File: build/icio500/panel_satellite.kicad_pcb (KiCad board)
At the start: 2 copper layers, 38.1 x 133.3 mm, 30 parts, among them J1 ?, U1 IS31FL3236

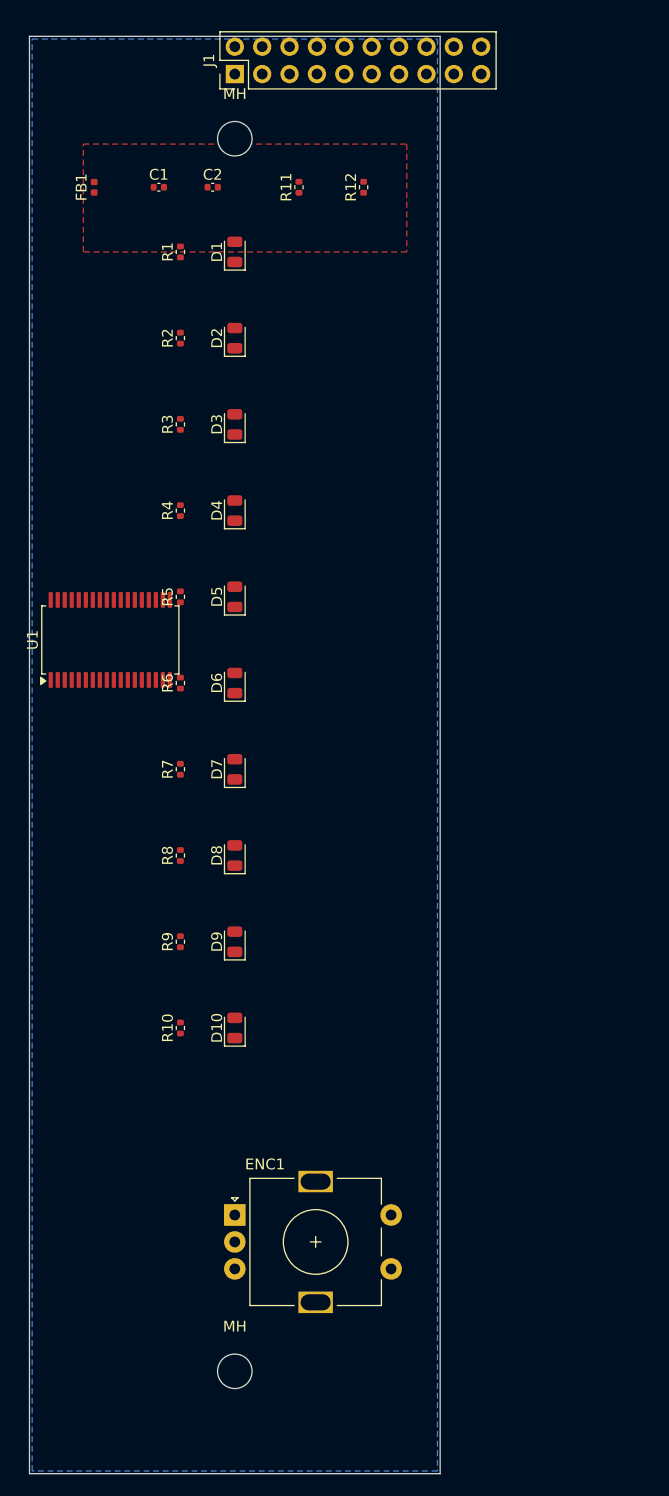
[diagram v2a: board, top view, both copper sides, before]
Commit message: Inject nets and auto-route 98% of satellite board
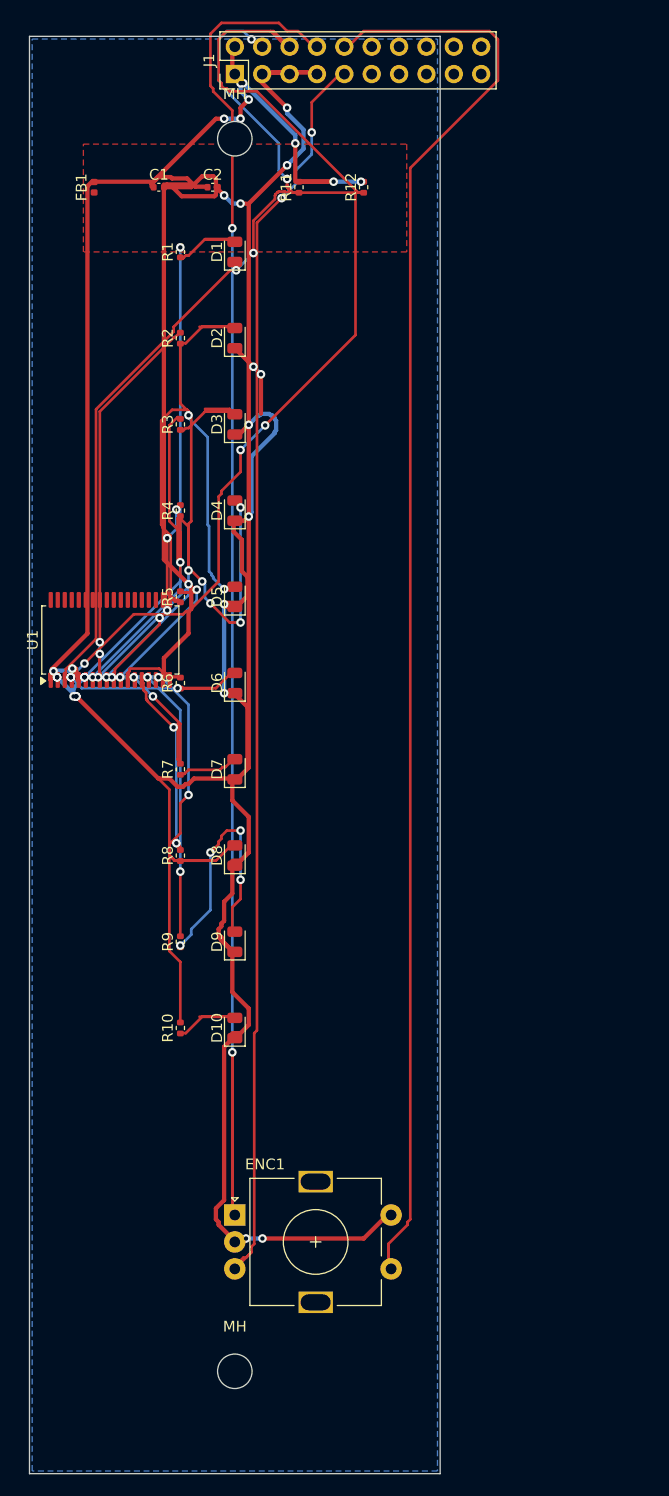
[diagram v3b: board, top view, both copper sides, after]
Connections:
- C1 pad 1: +3V3_CLEAN -> +3V3
- C2 pad 1: +3V3_CLEAN -> +3V3
- D1 pad 1: (no net) -> GND
- D1 pad 2: (no net) -> LED_1_MID
- D10 pad 1: (no net) -> GND
- D10 pad 2: (no net) -> LED_10_MID
- D2 pad 1: (no net) -> GND
- D2 pad 2: (no net) -> LED_2_MID
- D3 pad 1: (no net) -> GND
- D3 pad 2: (no net) -> LED_3_MID
- D4 pad 1: (no net) -> GND
- D4 pad 2: (no net) -> LED_4_MID
- D5 pad 1: (no net) -> GND
- D5 pad 2: (no net) -> LED_5_MID
- D6 pad 1: (no net) -> GND
- D6 pad 2: (no net) -> LED_6_MID
- D7 pad 1: (no net) -> GND
- D7 pad 2: (no net) -> LED_7_MID
- D8 pad 1: (no net) -> GND
- D8 pad 2: (no net) -> LED_8_MID
- D9 pad 1: (no net) -> GND
- D9 pad 2: (no net) -> LED_9_MID
- ENC1 pad A: (no net) -> ENC_A
- ENC1 pad B: (no net) -> ENC_B
- ENC1 pad C: (no net) -> GND
- ENC1 pad S1: (no net) -> ENC_SW
- ENC1 pad S2: (no net) -> GND
- FB1 pad 1: +3V3 -> +3V3_IN
- FB1 pad 2: +3V3_CLEAN -> +3V3
- J1 pad 1: daisy_5v_power -> +3V3
- J1 pad 10: gpio_enc_b -> ENC_SW
- J1 pad 11: gpio_enc_sw -> (no net)
- J1 pad 12: spi1_mosi -> (no net)
- J1 pad 13: spi1_miso -> (no net)
- J1 pad 14: spi1_sck -> (no net)
- J1 pad 15: spi1_cs -> (no net)
- J1 pad 16: gpio_disp_dc -> (no net)
- J1 pad 17: gpio_disp_res -> (no net)
- J1 pad 18: p18 -> (no net)
- J1 pad 19: p19 -> (no net)
- J1 pad 2: audio_in_r -> +3V3
- J1 pad 20: p20 -> (no net)
- J1 pad 3: gnd -> GND
- J1 pad 4: i2c1_sda -> SDA
- J1 pad 5: gnd -> GND
- J1 pad 6: i2c1_scl -> SCL
- J1 pad 7: gnd -> GND
- J1 pad 8: d13 -> ENC_A
- J1 pad 9: d14 -> ENC_B
- R1 pad 1: LED_1 -> LED_1_MID
- R1 pad 2: LED_1_A -> LED_1
- R10 pad 1: LED_10 -> LED_10_MID
- R10 pad 2: LED_10_A -> LED_10
- R11 pad 1: +3V3_CLEAN -> SDA
- R11 pad 2: SDA -> +3V3
- R12 pad 1: +3V3_CLEAN -> SCL
- R12 pad 2: SCL -> +3V3
- R2 pad 1: LED_2 -> LED_2_MID
- R2 pad 2: LED_2_A -> LED_2
- R3 pad 1: LED_3 -> LED_3_MID
- R3 pad 2: LED_3_A -> LED_3
- R4 pad 1: LED_4 -> LED_4_MID
- R4 pad 2: LED_4_A -> LED_4
- R5 pad 1: LED_5 -> LED_5_MID
- R5 pad 2: LED_5_A -> LED_5
- R6 pad 1: LED_6 -> LED_6_MID
- R6 pad 2: LED_6_A -> LED_6
- R7 pad 1: LED_7 -> LED_7_MID
- R7 pad 2: LED_7_A -> LED_7
- R8 pad 1: LED_8 -> LED_8_MID
- R8 pad 2: LED_8_A -> LED_8
- R9 pad 1: LED_9 -> LED_9_MID
- R9 pad 2: LED_9_A -> LED_9
- U1 pad 1: LED_9 -> +3V3
- U1 pad 10: GND -> LED_4
- U1 pad 11: SCL -> LED_5
- U1 pad 12: SDA -> LED_6
- U1 pad 13: +3V3_CLEAN -> LED_7
- U1 pad 14: GND -> LED_8
- U1 pad 15: +3V3_CLEAN -> LED_9
- U1 pad 16: +3V3_CLEAN -> LED_10
- U1 pad 17: GND -> (no net)
- U1 pad 18: GND -> (no net)
- U1 pad 19: LED_10 -> (no net)
- U1 pad 2: LED_8 -> GND
- U1 pad 3: LED_7 -> SDA
- U1 pad 4: LED_6 -> SCL
- U1 pad 5: LED_5 -> +3V3
- U1 pad 6: LED_4 -> GND
- U1 pad 7: LED_3 -> LED_1
- U1 pad 9: LED_1 -> LED_3
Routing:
- net GND: track 0.00 -> 224.6 mm
- net (no net): track 0.00 -> 167.0 mm
- net ENC_A: track 0.00 -> 136.2 mm
- net ENC_SW: track 0.00 -> 135.9 mm
- net ENC_B: track 0.00 -> 117.8 mm
- net +3V3: track 0.00 -> 102.3 mm
- net SCL: track 0.00 -> 89.7 mm
- net SDA: track 0.00 -> 78.9 mm
- net LED_1: track 0.00 -> 43.5 mm
- net LED_5_MID: track 0.00 -> 40.9 mm
- net LED_2: track 0.00 -> 37.9 mm
- net LED_10: track 0.00 -> 34.9 mm
- net LED_3: track 0.00 -> 28.6 mm
- net LED_9: track 0.00 -> 25.1 mm
- net LED_4_MID: track 0.00 -> 24.6 mm
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- added copper zone on B.Cu, net (none)
- added copper zone on F.Cu, net (none)
- removed copper zone on F.Cu, net +3V3_CLEAN
- removed copper zone on B.Cu, net GND

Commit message: Update satellite connector position and faceplate cutouts/silkscreen, regenerate STEP files
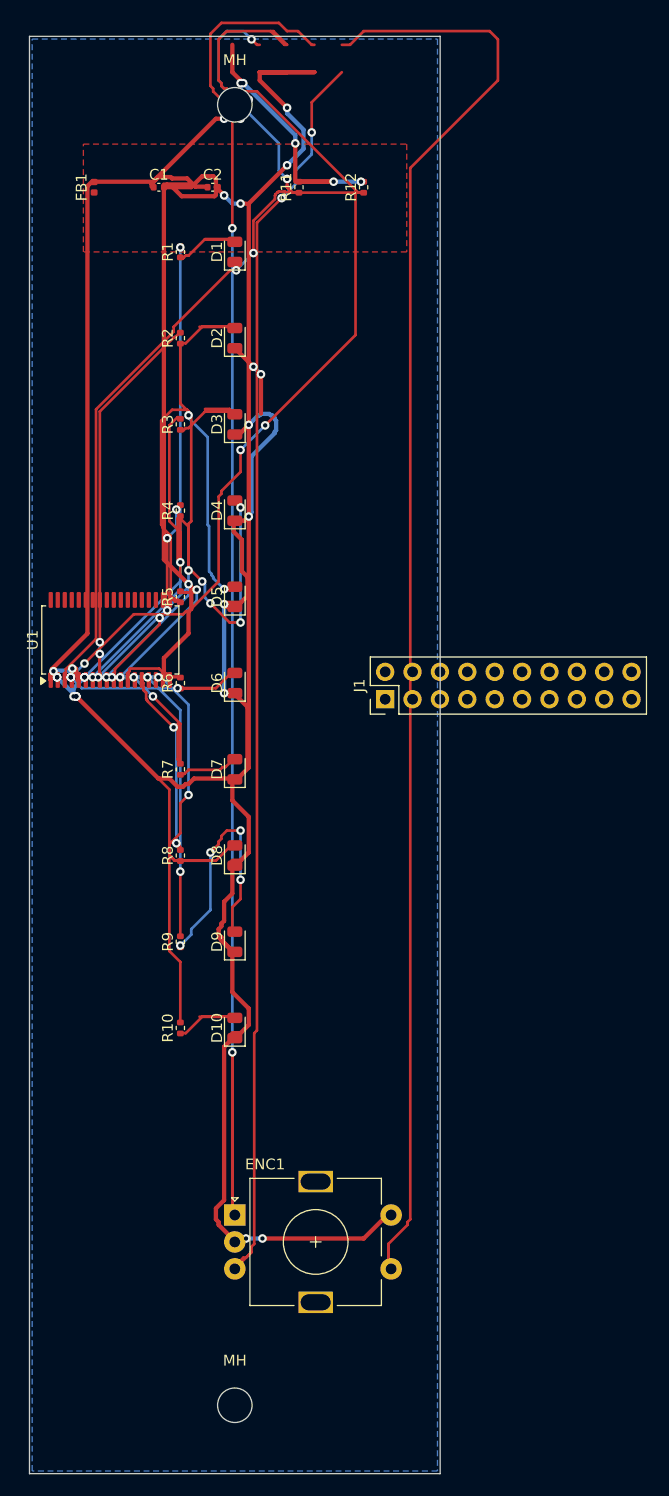
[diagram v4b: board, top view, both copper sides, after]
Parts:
- moved J1 59.7 mm to (133.0, 161.5)
- moved MH 3.15 mm to (119.0, 106.3)
- moved MH 3.15 mm to (119.0, 227.0)
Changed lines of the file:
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@@
 	(footprint "MountingHole_3.2mm_M3"
 		(layer "F.Cu")
-		(at 119.05 109.5)
+		(at 119.05 106.35)
 		(descr "Mounting Hole 3.2mm, M3, no annular, generated by kicad-footprint-generator mountinghole.py")
 		(tags "mountinghole M3")
@@
 	(footprint "Connector_PinHeader_2.54mm:PinHeader_2x10_P2.54mm_Vertical"
 		(layer "F.Cu")
-		(at 119.05 103.50 90)
+		(at 133.0 161.5 90)
 		(descr "Through hole straight pin header, 2x10, 2.54mm pitch, double rows")
 		(tags "Through hole pin header THT 2x10 2.54mm double row")
@@
 	(footprint "MountingHole_3.2mm_M3"
 		(layer "F.Cu")
-		(at 119.05 223.85)
+		(at 119.05 227.0)
 		(descr "Mounting Hole 3.2mm, M3, no annular, generated by kicad-footprint-generator mountinghole.py")
 		(tags "mountinghole M3")

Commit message: Optimize ribbon connector placement on both satellite and main boards for clean ribbon routing
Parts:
- moved R12 48.0 mm to (103.0, 153.0)
- moved R11 42.2 mm to (103.0, 150.0)
- moved J1 32.5 mm to (105.0, 178.0)
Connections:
- C1 pad 1: +3V3 -> (no net)
- C1 pad 2: GND -> (no net)
- C2 pad 1: +3V3 -> (no net)
- C2 pad 2: GND -> (no net)
- D1 pad 1: GND -> (no net)
- D1 pad 2: LED_1_MID -> (no net)
- D2 pad 1: GND -> (no net)
- D2 pad 2: LED_2_MID -> (no net)
- D3 pad 1: GND -> (no net)
- D3 pad 2: LED_3_MID -> (no net)
- D4 pad 1: GND -> (no net)
- D4 pad 2: LED_4_MID -> (no net)
- D5 pad 1: GND -> (no net)
- D5 pad 2: LED_5_MID -> (no net)
- D6 pad 1: GND -> (no net)
- D7 pad 1: GND -> (no net)
- D9 pad 1: GND -> (no net)
- ENC1 pad A: ENC_A -> (no net)
- ENC1 pad B: ENC_B -> (no net)
- ENC1 pad C: GND -> (no net)
- ENC1 pad S1: ENC_SW -> (no net)
- ENC1 pad S2: GND -> (no net)
- FB1 pad 1: +3V3_IN -> (no net)
- FB1 pad 2: +3V3 -> (no net)
- J1 pad 1: +3V3 -> (no net)
- J1 pad 10: ENC_SW -> (no net)
- J1 pad 2: +3V3 -> (no net)
- J1 pad 3: GND -> (no net)
- J1 pad 5: GND -> (no net)
- J1 pad 7: GND -> (no net)
- J1 pad 8: ENC_A -> (no net)
- J1 pad 9: ENC_B -> (no net)
- R1 pad 1: LED_1_MID -> (no net)
- R1 pad 2: LED_1 -> (no net)
- R11 pad 2: +3V3 -> (no net)
- R12 pad 2: +3V3 -> (no net)
- R4 pad 1: LED_4_MID -> (no net)
- R4 pad 2: LED_4 -> (no net)
- R5 pad 1: LED_5_MID -> (no net)
- R5 pad 2: LED_5 -> (no net)
- R6 pad 2: LED_6 -> (no net)
- U1 pad 1: +3V3 -> (no net)
- U1 pad 16: LED_10 -> (no net)
- U1 pad 2: GND -> (no net)
- U1 pad 5: +3V3 -> (no net)
- U1 pad 6: GND -> (no net)
- U1 pad 7: LED_1 -> (no net)
- U1 pad 8: LED_2 -> (no net)
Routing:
- net GND: track 224.6 -> 20.9 mm
- net (no net): track 167.0 -> 0.00 mm
- net ENC_A: track 136.2 -> 0.00 mm
- net ENC_SW: track 135.9 -> 0.00 mm
- net ENC_B: track 117.8 -> 0.00 mm
- net +3V3: track 102.3 -> 0.00 mm
- net SCL: track 89.7 -> 12.0 mm
- net SDA: track 78.9 -> 11.4 mm
- net LED_1: track 43.5 -> 0.00 mm
- net LED_5_MID: track 40.9 -> 0.00 mm
- net LED_2: track 37.9 -> 0.00 mm
- net LED_10: track 34.9 -> 0.00 mm
- net LED_4_MID: track 24.6 -> 0.00 mm
- net LED_4: track 19.0 -> 0.00 mm
- net LED_8: track 18.1 -> 0.00 mm
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
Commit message: Fix orientation of ribbon connectors to prevent them from hanging off the PCB
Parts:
- moved J1 3.00 mm to (105.0, 175.0), turned to 0 degrees
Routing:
- net LED_3: track 27.6 -> 0.00 mm
- net LED_9: track 25.0 -> 0.00 mm
- net GND: track 20.9 -> 0.00 mm
- net LED_7: track 13.2 -> 0.00 mm
- net SCL: track 12.0 -> 0.00 mm
- net SDA: track 11.4 -> 0.00 mm
- net LED_9_MID: track 9.06 -> 0.00 mm
- net LED_7_MID: track 9.06 -> 0.00 mm
- net LED_8_MID: track 9.06 -> 0.00 mm
- net LED_6_MID: track 9.06 -> 0.00 mm
- net LED_10_MID: track 8.58 -> 0.00 mm
- net 0: vias 8 -> 0

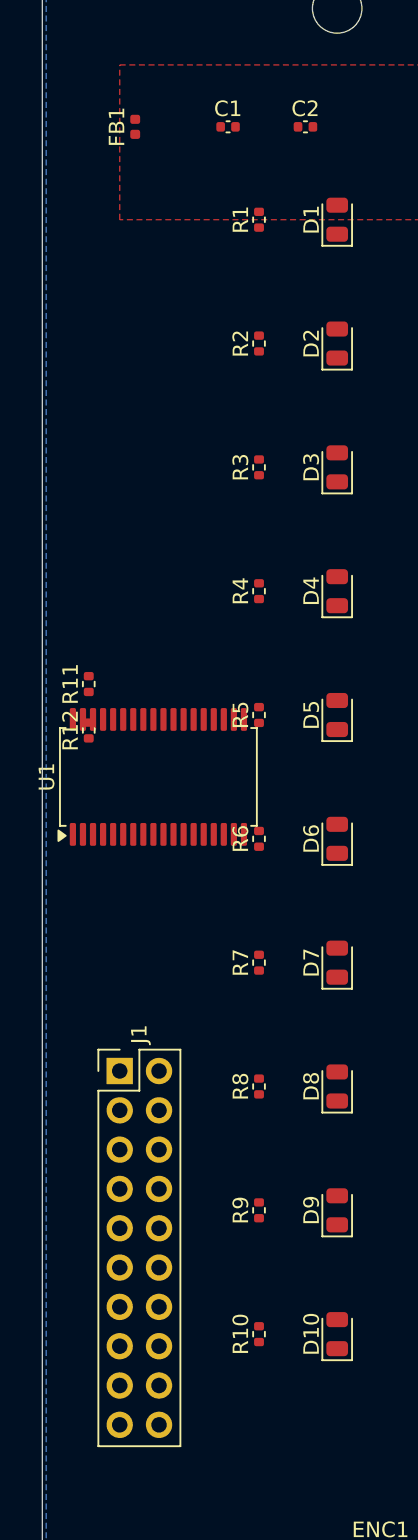
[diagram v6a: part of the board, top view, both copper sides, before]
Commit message: Convert satellite ribbon connector to SMD and flip all back-side components to B.Cu
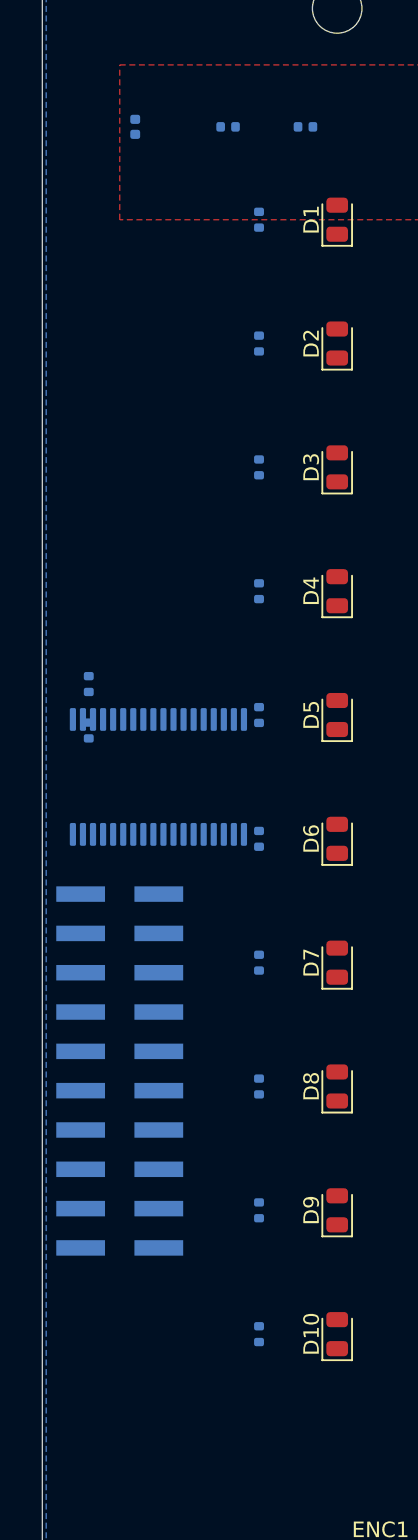
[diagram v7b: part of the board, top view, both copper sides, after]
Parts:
- C1, C2, FB1, R1, R10, R11, R12, R2, R3, R4, R5, R6, R7, R8, R9, U1: moved to B.Cu
- J1: value ? -> Conn_02x10_Odd_Even; footprint Connector_PinHeader_2.54mm:PinHeader_2x10_P2.54mm_Vertical -> Connector_PinHeader_2.54mm:PinHeader_2x10_P2.54mm_Vertical_SMD; moved to B.Cu
- turned C1 to 180 degrees
- turned C2 to 180 degrees
- turned J1 to 180 degrees
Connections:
- J1 pad 4: SDA -> (no net)
- J1 pad 6: SCL -> (no net)

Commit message: Refactor mechanical assembly: Use direct right-angle header connection between main board and satellite board, eliminating the ribbon cable
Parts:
- J1: footprint Connector_PinHeader_2.54mm:PinHeader_2x10_P2.54mm_Vertical_SMD -> Connector_PinSocket_2.54mm:PinSocket_2x10_P2.54mm_Vertical_SMD
- moved J1 14.0 mm to (119.0, 175.0), turned to 0 degrees
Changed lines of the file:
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@@
 		)
 	)
-	(footprint "Connector_PinHeader_2.54mm:PinHeader_2x10_P2.54mm_Vertical_SMD"
+	(footprint "Connector_PinSocket_2.54mm:PinSocket_2x10_P2.54mm_Vertical_SMD"
 		(layer "B.Cu")
-		(at 105 175 180)
+		(at 119.05 175.0 0)
 		(descr "surface-mounted straight pin header, 2x10, 2.54mm pitch, double rows")
 		(tags "Surface mounted pin header SMD 2x10 2.54mm double row")
@@
 		)
 		(embedded_fonts no)
-		(model "${KICAD10_3DMODEL_DIR}/Connector_PinHeader_2.54mm.3dshapes/PinHeader_2x10_P2.54mm_Vertical_SMD.step"
+		(model "${KICAD10_3DMODEL_DIR}/Connector_PinSocket_2.54mm.3dshapes/PinSocket_2x10_P2.54mm_Vertical_SMD.step"
 			(offset
 				(xyz 0 0 0)
